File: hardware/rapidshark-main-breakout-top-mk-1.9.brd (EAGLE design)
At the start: 44 x 18 mm, 10 parts, among them U1 ADAFRUIT_METRO_MININOSILK-AMB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

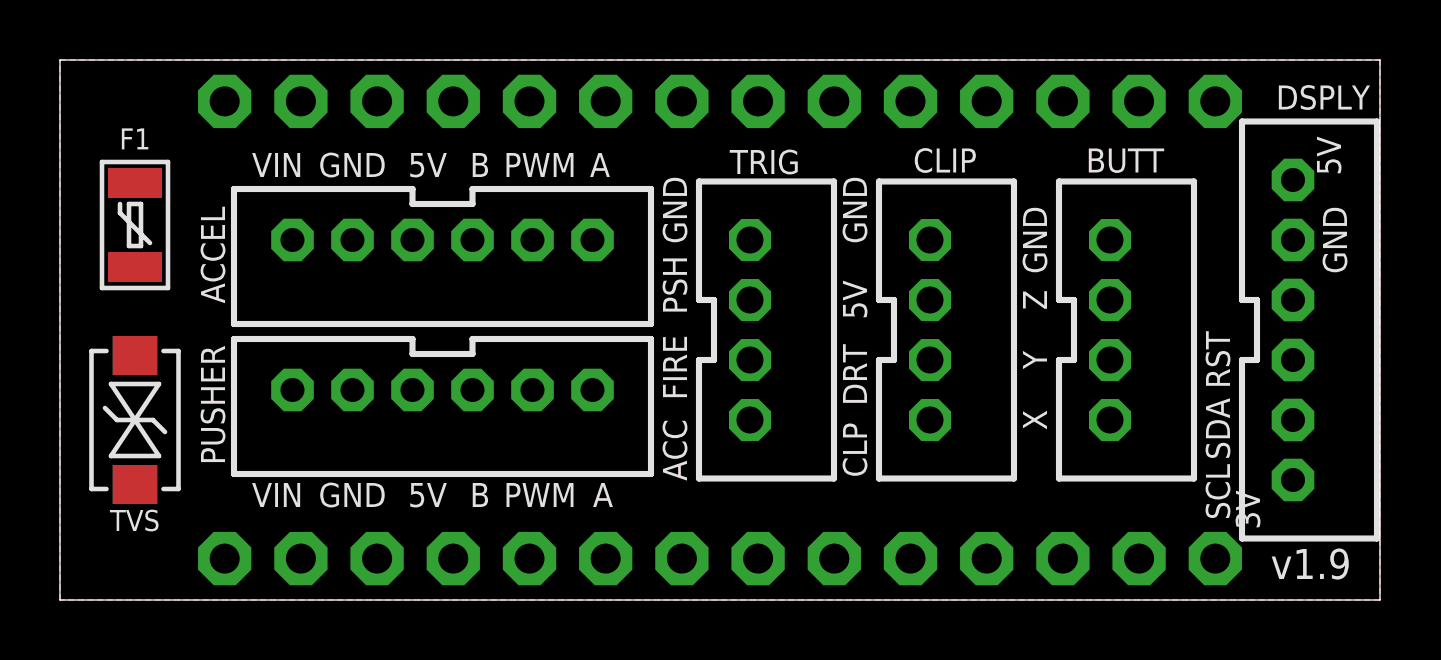
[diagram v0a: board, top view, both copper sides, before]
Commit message: tweaks to jst part hole sizes
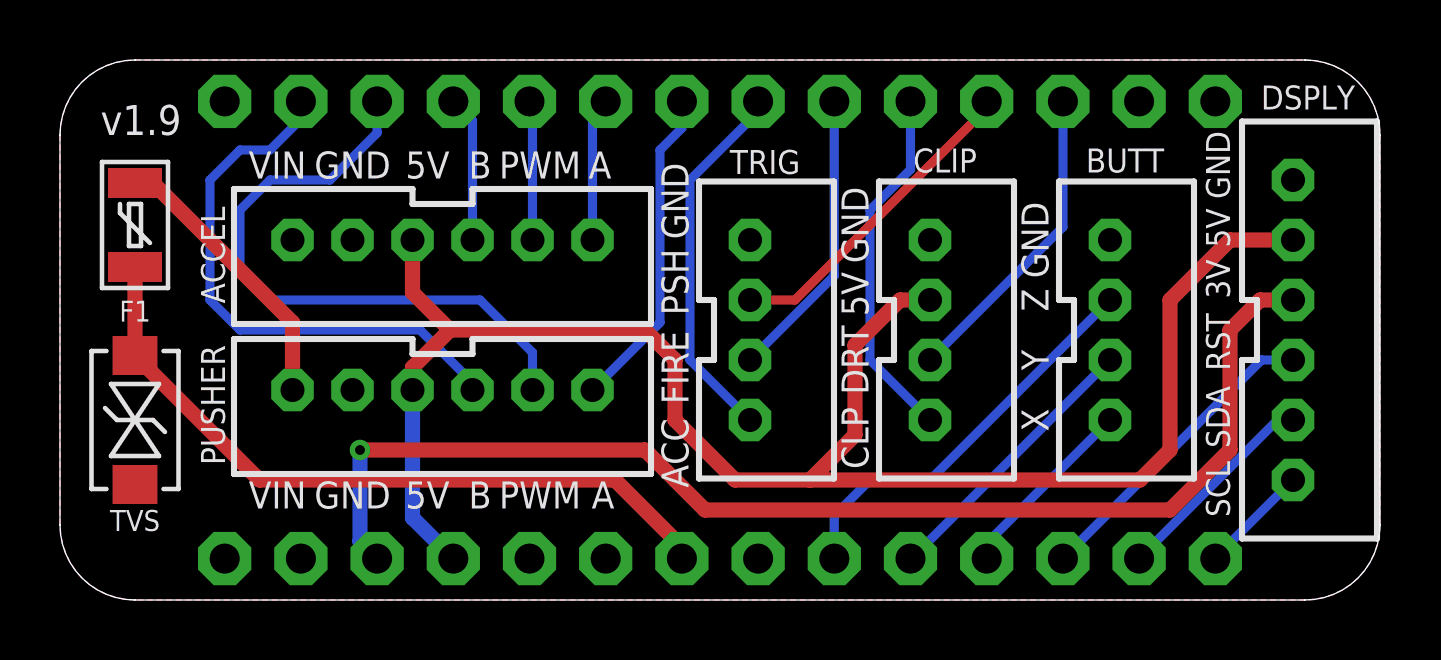
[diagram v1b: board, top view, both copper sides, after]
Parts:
- F1: value 100mA -> 120mA
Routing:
- net 5V: track 0.00 -> 58.0 mm
- net 3.3V: track 0.00 -> 41.0 mm, vias 0 -> 1
- net N$1: track 0.00 -> 24.2 mm
- net PUSH_PWM: track 0.00 -> 20.8 mm
- net PUSH_B: track 0.00 -> 18.6 mm
- net Z: track 0.00 -> 13.6 mm
- net ACCEL: track 0.00 -> 12.4 mm
- net CLIP: track 0.00 -> 12.0 mm
- net PUSH_A: track 0.00 -> 10.9 mm
- net PUSH: track 0.00 -> 10.8 mm
- net DART: track 0.00 -> 10.5 mm
- net DISP_RST: track 0.00 -> 10.4 mm
- net FIRE: track 0.00 -> 9.78 mm
- net VIN: track 0.00 -> 9.43 mm
- net Y: track 0.00 -> 9.39 mm
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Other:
- outline, holes or cut-outs redrawn
- board text removed: "BARREL"
- board text removed: "BUTT"
- board text removed: "DOWN"
- board text removed: "UP"

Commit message: relayout and now provides both 3V and 5V to display (but assumes IO voltage is whatever the arduino sends out
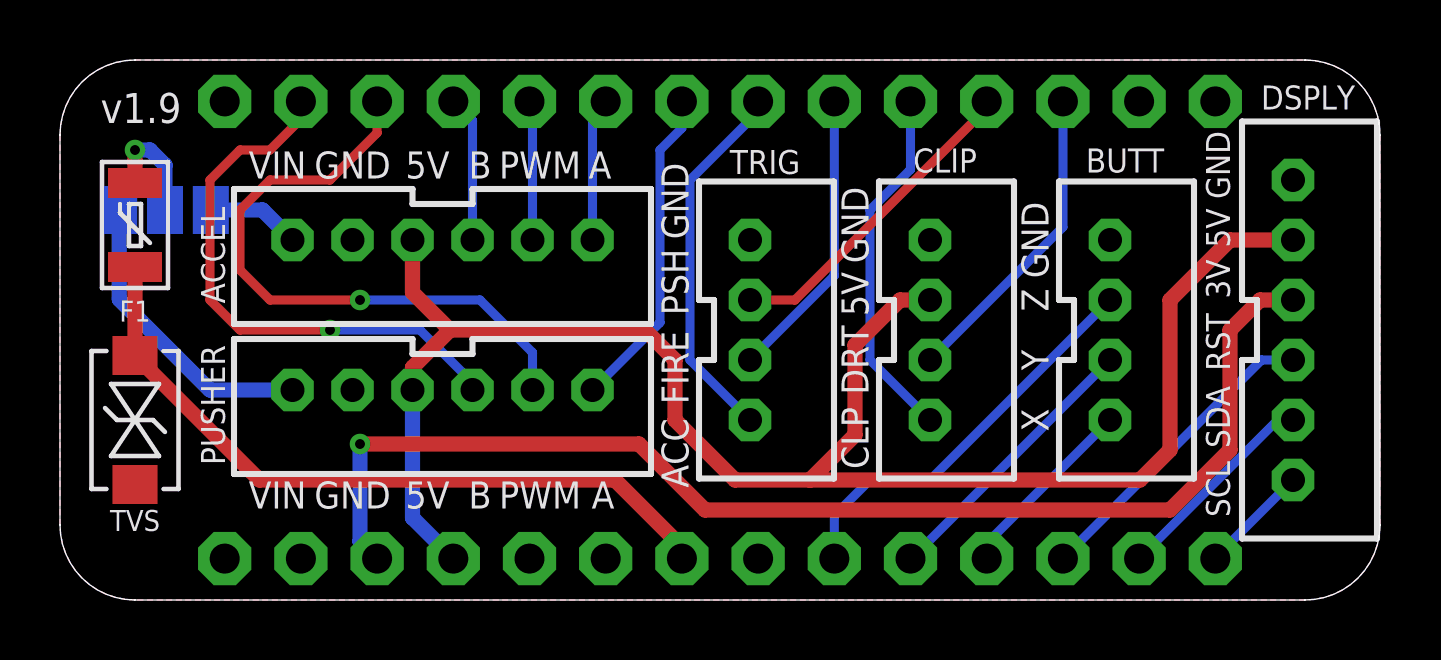
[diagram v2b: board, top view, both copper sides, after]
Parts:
- added U$2: (no value), A_butts:COW_SMALL
- added U$3: (no value), A_butts:OSHWLOGO_TINY_SILKONLY
- added VIN: (no value), A_butts:PAD-JUMPER-3-NO_YES_SILK_FULL_BOX
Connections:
- new net VIN_ACCEL: ACCEL.6, VIN.3
- new net VIN_PUSHER: PUSHER.6, VIN.1
- net VIN: now also VIN.2; no longer PUSHER.6
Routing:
- net VIN_PUSHER: track 0.00 -> 10.0 mm
- net VIN: track 9.43 -> 3.81 mm, vias 0 -> 1
- net VIN_ACCEL: track 0.00 -> 3.14 mm
- net PUSH_PWM: vias 0 -> 1
- net PUSH_B: vias 0 -> 1
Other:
- board text added: "RapidShark Breakout"
- board text added: "by schizobovine <sean@yak.net>"
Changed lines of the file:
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@@
 <setting verticaltext="up"/>
 </settings>
-<grid distance="0.5" unitdist="mm" unit="mm" style="lines" multiple="2" display="yes" altdistance="1" altunitdist="mil" altunit="mil"/>
+<grid distance="0.1" unitdist="mm" unit="mm" style="lines" multiple="5" display="yes" altdistance="1" altunitdist="mil" altunit="mil"/>
 <layers>
 <layer number="1" name="Top" color="4" fill="1" visible="yes" active="yes"/>
@@
 <wire x1="0" y1="2.5" x2="0" y2="15.5" width="0" layer="20"/>
 <wire x1="0" y1="15.5" x2="2.5" y2="18" width="0" layer="20" curve="-90"/>
-<text x="2.7" y="16" size="1" layer="21" font="vector" ratio="16" rot="R180" align="center">&gt;VERSION</text>
-<text x="2.7" y="16" size="1" layer="1" font="vector" ratio="16" rot="R180" align="center">&gt;VERSION</text>
+<text x="2.7" y="16.4" size="1" layer="21" font="vector" ratio="16" rot="R180" align="center">&gt;VERSION</text>
+<text x="2.7" y="16.4" size="1" layer="1" font="vector" ratio="16" rot="R180" align="center">&gt;VERSION</text>
 <text x="9.75" y="3.5" size="0.9" layer="21" font="vector" ratio="12" rot="R180" align="center">GND</text>
 <text x="7.25" y="3.5" size="0.9" layer="21" font="vector" ratio="12" rot="R180" align="center">VIN</text>
@@
 <text x="18" y="14.5" size="0.9" layer="21" font="vector" ratio="12" rot="R180" align="center">A</text>
 <text x="38.6" y="10.7" size="0.8" layer="21" font="vector" ratio="12" rot="R270" align="center">3V</text>
+<text x="12.75" y="7.9" size="1.27" layer="22" font="vector" ratio="12" rot="MR0" align="bottom-center">RapidShark
+Breakout</text>
+<text x="23" y="4.3" size="1" layer="22" font="vector" ratio="12" rot="MR0" align="bottom-center">by schizobovine &lt;sean@yak.net&gt;</text>
+<text x="2.5" y="2" size="1" layer="22" font="vector" ratio="16" rot="MR180" align="center">&gt;VERSION</text>
+<text x="2.5" y="2" size="1" layer="16" font="vector" ratio="16" rot="MR180" align="center">&gt;VERSION</text>
 </plain>
 <attributes>
@@
 <attribute name="NAME" x="41.6" y="16.35" size="0.8" layer="25" font="vector" ratio="12" rot="R180" align="top-center"/>
 </element>
+<element name="U$2" library="A_butts" package="COW_SMALL" value="" x="3.5" y="8.5" rot="MR0"/>
+<element name="U$3" library="A_butts" package="OSHWLOGO_TINY_SILKONLY" value="" x="41.2" y="1.7" rot="MR0"/>
+<element name="VIN" library="A_butts" package="PAD-JUMPER-3-NO_YES_SILK_FULL_BOX" value="" x="3.5" y="13" smashed="yes" rot="MR180">
+<attribute name="NAME" x="3.5" y="15.05" size="0.8" layer="26" font="vector" ratio="12" rot="SMR180" align="bottom-center"/>
+<attribute name="VALUE" x="3.5" y="14.25" size="0.6" layer="28" font="vector" ratio="12" rot="MR180" align="top-center"/>
+</element>
 </elements>
 <signals>
@@
 <contactref element="DSPLY" pad="3"/>
 <wire x1="10.57" y1="1.38" x2="10" y2="1.95" width="0.508" layer="16"/>
-<wire x1="10" y1="1.95" x2="10" y2="5" width="0.508" layer="16"/>
-<via x="10" y="5" extent="1-16" drill="0.3302"/>
-<wire x1="10" y1="5" x2="19.5" y2="5" width="0.508" layer="1"/>
-<wire x1="19.5" y1="5" x2="21.5" y2="3" width="0.508" layer="1"/>
+<wire x1="10" y1="1.95" x2="10" y2="5.2" width="0.508" layer="16"/>
+<via x="10" y="5.2" extent="1-16" drill="0.3302"/>
+<wire x1="10" y1="5.2" x2="19.3" y2="5.2" width="0.508" layer="1"/>
+<wire x1="19.3" y1="5.2" x2="21.5" y2="3" width="0.508" layer="1"/>
 <wire x1="21.5" y1="3" x2="37" y2="3" width="0.508" layer="1"/>
 <wire x1="37" y1="3" x2="39" y2="5" width="0.508" layer="1"/>
@@
 <signal name="VIN">
 <contactref element="F1" pad="2"/>
-<contactref element="PUSHER" pad="6"/>
-<wire x1="7.75" y1="7" x2="7.75" y2="9.25" width="0.508" layer="1"/>
-<wire x1="7.75" y1="9.25" x2="3.1" y2="13.9" width="0.508" layer="1"/>
-<wire x1="3.1" y1="13.9" x2="2.5" y2="13.9" width="0.508" layer="1"/>
+<contactref element="VIN" pad="2"/>
+<wire x1="3.5" y1="13" x2="3.5" y2="14.5" width="0.508" layer="16"/>
+<wire x1="3.5" y1="14.5" x2="3" y2="15" width="0.508" layer="16"/>
+<wire x1="3" y1="15" x2="2.5" y2="15" width="0.508" layer="16"/>
+<via x="2.5" y="15" extent="1-16" drill="0.3302"/>
+<wire x1="2.5" y1="15" x2="2.5" y2="13.9" width="0.508" layer="1"/>
 </signal>
 <signal name="PUSH_A">
@@
 <wire x1="15.75" y1="7" x2="15.75" y2="8.25" width="0.3048" layer="16"/>
 <wire x1="15.75" y1="8.25" x2="14" y2="10" width="0.3048" layer="16"/>
-<wire x1="14" y1="10" x2="7" y2="10" width="0.3048" layer="16"/>
-<wire x1="7" y1="10" x2="6" y2="11" width="0.3048" layer="16"/>
-<wire x1="6" y1="11" x2="6" y2="13" width="0.3048" layer="16"/>
-<wire x1="6" y1="13" x2="7" y2="14" width="0.3048" layer="16"/>
-<wire x1="7" y1="14" x2="9" y2="14" width="0.3048" layer="16"/>
-<wire x1="9" y1="14" x2="10.57" y2="15.57" width="0.3048" layer="16"/>
-<wire x1="10.57" y1="15.57" x2="10.57" y2="16.62" width="0.3048" layer="16"/>
+<wire x1="14" y1="10" x2="10" y2="10" width="0.3048" layer="16"/>
+<wire x1="10" y1="10" x2="7" y2="10" width="0.3048" layer="1"/>
+<wire x1="7" y1="10" x2="6" y2="11" width="0.3048" layer="1"/>
+<wire x1="6" y1="11" x2="6" y2="13" width="0.3048" layer="1"/>
+<wire x1="6" y1="13" x2="7" y2="14" width="0.3048" layer="1"/>
+<wire x1="7" y1="14" x2="9" y2="14" width="0.3048" layer="1"/>
+<wire x1="9" y1="14" x2="10.57" y2="15.57" width="0.3048" layer="1"/>
+<wire x1="10.57" y1="15.57" x2="10.57" y2="16.62" width="0.3048" layer="1"/>
+<via x="10" y="10" extent="1-16" drill="0.3302"/>
 </signal>
 <signal name="PUSH_B">
@@
 <wire x1="13.75" y1="7" x2="13.75" y2="7.25" width="0.3048" layer="16"/>
 <wire x1="13.75" y1="7.25" x2="12" y2="9" width="0.3048" layer="16"/>
-<wire x1="12" y1="9" x2="6" y2="9" width="0.3048" layer="16"/>
-<wire x1="6" y1="9" x2="5" y2="10" width="0.3048" layer="16"/>
-<wire x1="5" y1="10" x2="5" y2="14" width="0.3048" layer="16"/>
-<wire x1="5" y1="14" x2="6" y2="15" width="0.3048" layer="16"/>
-<wire x1="6" y1="15" x2="7" y2="15" width="0.3048" layer="16"/>
-<wire x1="7" y1="15" x2="8.03" y2="16.03" width="0.3048" layer="16"/>
-<wire x1="8.03" y1="16.03" x2="8.03" y2="16.62" width="0.3048" layer="16"/>
+<wire x1="12" y1="9" x2="9" y2="9" width="0.3048" layer="16"/>
+<wire x1="9" y1="9" x2="6" y2="9" width="0.3048" layer="1"/>
+<wire x1="6" y1="9" x2="5" y2="10" width="0.3048" layer="1"/>
+<wire x1="5" y1="10" x2="5" y2="14" width="0.3048" layer="1"/>
+<wire x1="5" y1="14" x2="6" y2="15" width="0.3048" layer="1"/>
+<wire x1="6" y1="15" x2="7" y2="15" width="0.3048" layer="1"/>
+<wire x1="7" y1="15" x2="8.03" y2="16.03" width="0.3048" layer="1"/>
+<wire x1="8.03" y1="16.03" x2="8.03" y2="16.62" width="0.3048" layer="1"/>
+<via x="9" y="9" extent="1-16" drill="0.3302"/>
 </signal>
 <signal name="ACCEL_A">
@@
 <wire x1="25.81" y1="2.81" x2="25.81" y2="1.38" width="0.3048" layer="16"/>
 </signal>
+<signal name="VIN_PUSHER">
+<contactref element="PUSHER" pad="6"/>
+<contactref element="VIN" pad="1"/>
+<wire x1="1.976" y1="13" x2="1.976" y2="10.024" width="0.508" layer="16"/>
+<wire x1="1.976" y1="10.024" x2="5" y2="7" width="0.508" layer="16"/>
+<wire x1="5" y1="7" x2="7.75" y2="7" width="0.508" layer="16"/>
+</signal>
+<signal name="VIN_ACCEL">
+<contactref element="ACCEL" pad="6"/>
+<contactref element="VIN" pad="3"/>
+<wire x1="7.75" y1="12" x2="6.75" y2="13" width="0.508" layer="16"/>
+<wire x1="6.75" y1="13" x2="5.024" y2="13" width="0.508" layer="16"/>
+</signal>
 </signals>
 </board>
 </drawing>
+<compatibility>
+<note version="6.3" minversion="6.2.2" severity="warning">
+Since Version 6.2.2 text objects can contain more than one line,
+which will not be processed correctly with this version.
+</note>
+</compatibility>
 </eagle>
